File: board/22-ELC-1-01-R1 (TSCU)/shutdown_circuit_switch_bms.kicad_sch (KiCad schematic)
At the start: 7 parts, among them Q14 AO3400A

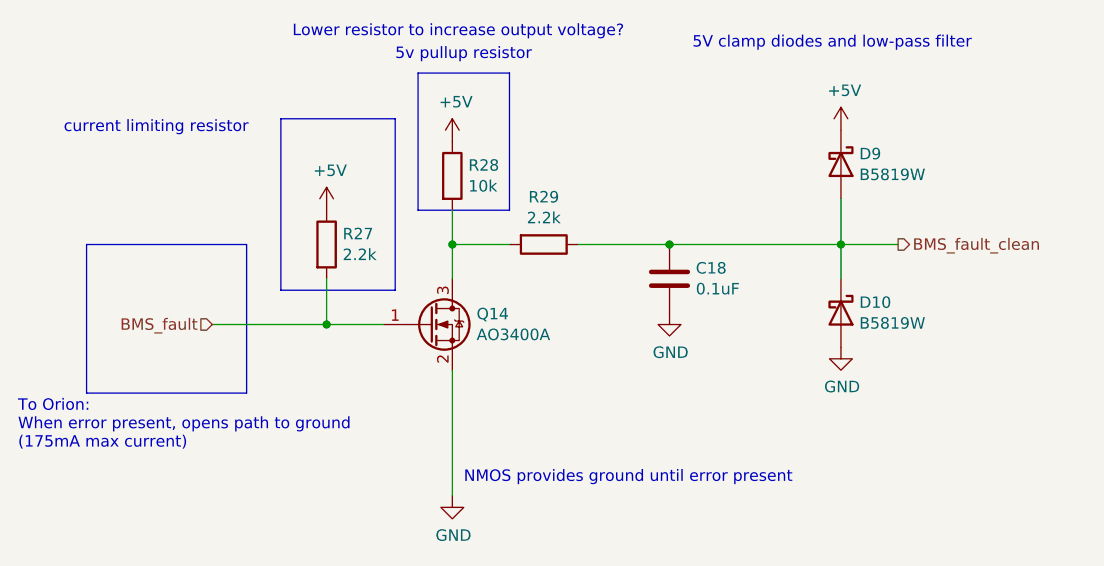
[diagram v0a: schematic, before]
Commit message: Added few LEDs
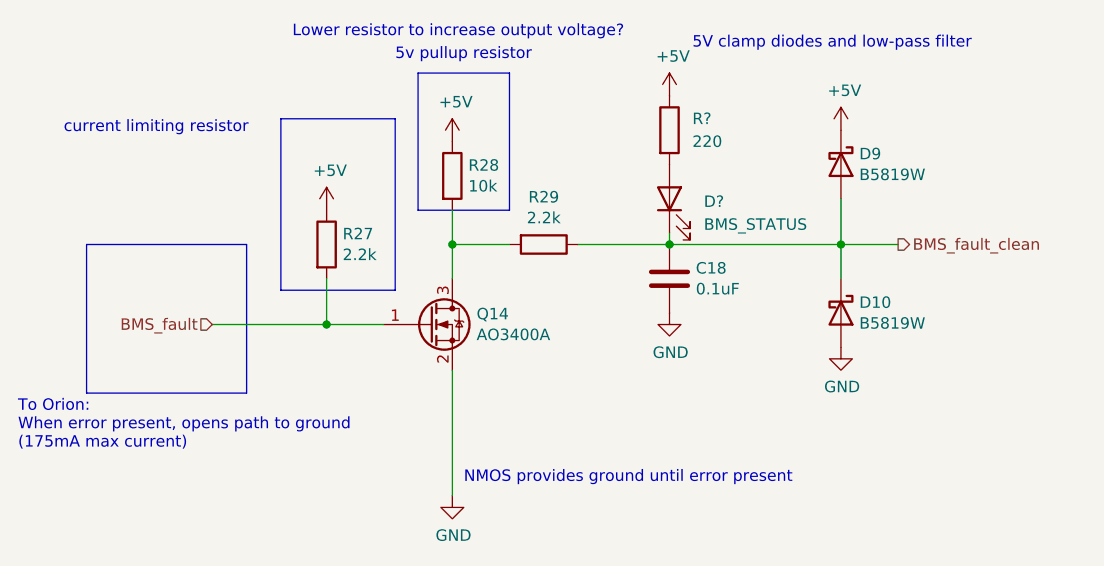
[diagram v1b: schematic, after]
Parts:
- added D?: BMS_STATUS, symbol Device:LED
- added R?: 220, symbol Device:R
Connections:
- net +5V: now also R?.1
- net BMS_fault_clean: now also D?.1 (K)
- new net: D?.2 (A), R?.2
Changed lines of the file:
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@@
+    (stroke (width 0) (type default) (color 0 0 0 0))
+  )
+  (wire (pts (xy 88.9 91.44) (xy 88.9 92.71))
     (stroke (width 0) (type default) (color 0 0 0 0))
   )
@@
     (pin "2")
   )
+  (symbol (lib_id "Device:LED") (at 88.9 87.63 90) (unit 1)
+    (in_bom yes) (on_board yes) (fields_autoplaced)
+    (property "Reference" "D?" (id 0) (at 92.71 87.9474 90)
+      (effects (font (size 1.27 1.27)) (justify right))
+    )
+    (property "Value" "BMS_STATUS" (id 1) (at 92.71 90.4874 90)
+      (effects (font (size 1.27 1.27)) (justify right))
+    )
+    (property "Footprint" "" (id 2) (at 88.9 87.63 0)
+      (effects (font (size 1.27 1.27)) hide)
+    )
+    (property "Datasheet" "~" (id 3) (at 88.9 87.63 0)
+      (effects (font (size 1.27 1.27)) hide)
+    )
+    (pin "1")
+    (pin "2")
+  )
+  (symbol (lib_id "Device:R") (at 88.9 80.01 0) (unit 1)
+    (in_bom yes) (on_board yes) (fields_autoplaced)
+    (property "Reference" "R?" (id 0) (at 91.44 78.7399 0)
+      (effects (font (size 1.27 1.27)) (justify left))
+    )
+    (property "Value" "220" (id 1) (at 91.44 81.2799 0)
+      (effects (font (size 1.27 1.27)) (justify left))
+    )
+    (property "Footprint" "" (id 2) (at 87.122 80.01 90)
+      (effects (font (size 1.27 1.27)) hide)
+    )
+    (property "Datasheet" "~" (id 3) (at 88.9 80.01 0)
+      (effects (font (size 1.27 1.27)) hide)
+    )
+    (pin "1")
+    (pin "2")
+  )
+  (symbol (lib_id "power:+5V") (at 88.9 76.2 0) (unit 1)
+    (in_bom yes) (on_board yes)
+    (property "Reference" "#PWR?" (id 0) (at 88.9 80.01 0)
+      (effects (font (size 1.27 1.27)) hide)
+    )
+    (property "Value" "+5V" (id 1) (at 89.281 71.8058 0))
+    (property "Footprint" "" (id 2) (at 88.9 76.2 0)
+      (effects (font (size 1.27 1.27)) hide)
+    )
+    (property "Datasheet" "" (id 3) (at 88.9 76.2 0)
+      (effects (font (size 1.27 1.27)) hide)
+    )
+    (pin "1")
+  )
 )

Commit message: More LEDs and test points
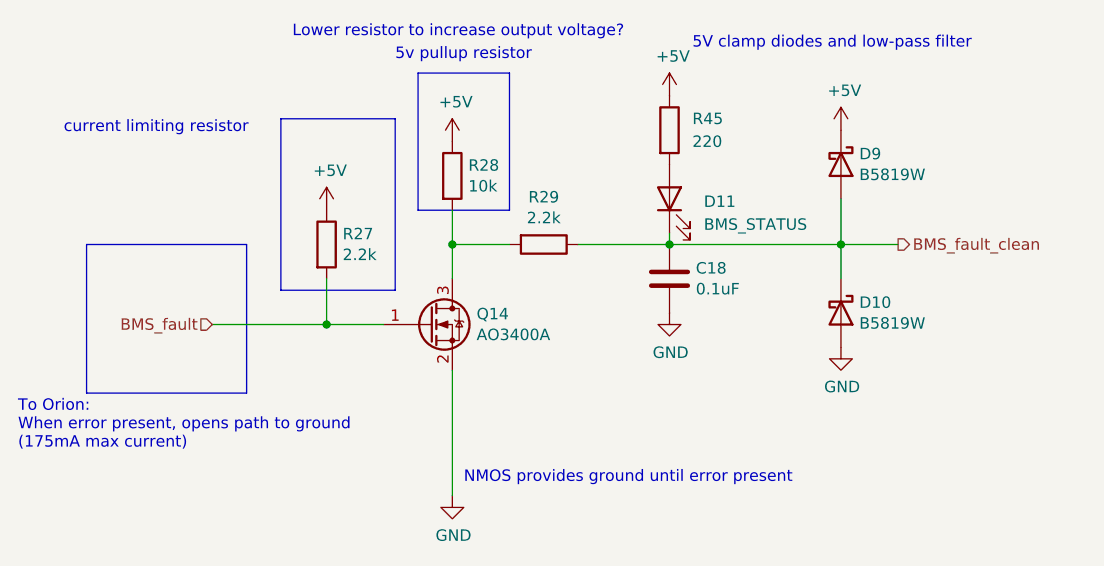
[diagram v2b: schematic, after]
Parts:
- gave numbers to parts that had none: 2
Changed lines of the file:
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@@
   (symbol (lib_id "Device:LED") (at 88.9 87.63 90) (unit 1)
     (in_bom yes) (on_board yes) (fields_autoplaced)
-    (property "Reference" "D?" (id 0) (at 92.71 87.9474 90)
+    (property "Reference" "D11" (id 0) (at 92.71 87.9474 90)
       (effects (font (size 1.27 1.27)) (justify right))
     )
@@
   (symbol (lib_id "Device:R") (at 88.9 80.01 0) (unit 1)
     (in_bom yes) (on_board yes) (fields_autoplaced)
-    (property "Reference" "R?" (id 0) (at 91.44 78.7399 0)
+    (property "Reference" "R45" (id 0) (at 91.44 78.7399 0)
       (effects (font (size 1.27 1.27)) (justify left))
     )
@@
   (symbol (lib_id "power:+5V") (at 88.9 76.2 0) (unit 1)
     (in_bom yes) (on_board yes)
-    (property "Reference" "#PWR?" (id 0) (at 88.9 80.01 0)
+    (property "Reference" "#PWR0104" (id 0) (at 88.9 80.01 0)
       (effects (font (size 1.27 1.27)) hide)
     )

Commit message: Ready for review
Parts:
- renumbered C18 to C1, D11 to D2, D9 to D3, D10 to D4, Q14 to Q1, R27 to R1, R28 to R2, R29 to R3, R45 to R4
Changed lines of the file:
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@@
   (symbol (lib_id "power:+5V") (at 50.8 88.9 0) (unit 1)
     (in_bom yes) (on_board yes)
-    (property "Reference" "#PWR02" (id 0) (at 50.8 92.71 0)
+    (property "Reference" "#PWR010" (id 0) (at 50.8 92.71 0)
       (effects (font (size 1.27 1.27)) hide)
     )
@@
   (symbol (lib_id "Device:R") (at 50.8 92.71 0) (unit 1)
     (in_bom yes) (on_board yes)
-    (property "Reference" "R27" (id 0) (at 52.578 91.5416 0)
+    (property "Reference" "R1" (id 0) (at 52.578 91.5416 0)
       (effects (font (size 1.27 1.27)) (justify left))
     )
@@
   (symbol (lib_id "Device:R") (at 74.93 92.71 270) (unit 1)
     (in_bom yes) (on_board yes)
-    (property "Reference" "R29" (id 0) (at 74.93 87.4522 90))
+    (property "Reference" "R3" (id 0) (at 74.93 87.4522 90))
     (property "Value" "2.2k" (id 1) (at 74.93 89.7636 90))
     (property "Footprint" "Resistor_SMD:R_0603_1608Metric_Pad0.98x0.95mm_HandSolder" (id 2) (at 74.93 90.932 90)
@@
   (symbol (lib_id "Device:C") (at 88.9 96.52 0) (unit 1)
     (in_bom yes) (on_board yes)
-    (property "Reference" "C18" (id 0) (at 91.821 95.3516 0)
+    (property "Reference" "C1" (id 0) (at 91.821 95.3516 0)
       (effects (font (size 1.27 1.27)) (justify left))
     )
@@
   (symbol (lib_id "power:GND") (at 88.9 100.33 0) (unit 1)
     (in_bom yes) (on_board yes)
-    (property "Reference" "#PWR076" (id 0) (at 88.9 106.68 0)
+    (property "Reference" "#PWR014" (id 0) (at 88.9 106.68 0)
       (effects (font (size 1.27 1.27)) hide)
     )
@@
   (symbol (lib_id "power:GND") (at 107.95 104.14 0) (unit 1)
     (in_bom yes) (on_board yes)
-    (property "Reference" "#PWR079" (id 0) (at 107.95 110.49 0)
+    (property "Reference" "#PWR016" (id 0) (at 107.95 110.49 0)
       (effects (font (size 1.27 1.27)) hide)
     )
@@
   (symbol (lib_id "power:+5V") (at 107.95 80.01 0) (unit 1)
     (in_bom yes) (on_board yes)
-    (property "Reference" "#PWR078" (id 0) (at 107.95 83.82 0)
+    (property "Reference" "#PWR015" (id 0) (at 107.95 83.82 0)
       (effects (font (size 1.27 1.27)) hide)
     )
@@
   (symbol (lib_id "power:GND") (at 64.77 120.65 0) (unit 1)
     (in_bom yes) (on_board yes)
-    (property "Reference" "#PWR074" (id 0) (at 64.77 127 0)
+    (property "Reference" "#PWR012" (id 0) (at 64.77 127 0)
       (effects (font (size 1.27 1.27)) hide)
     )
@@
   (symbol (lib_id "Device:R") (at 64.77 85.09 0) (unit 1)
     (in_bom yes) (on_board yes)
-    (property "Reference" "R28" (id 0) (at 66.548 83.9216 0)
+    (property "Reference" "R2" (id 0) (at 66.548 83.9216 0)
       (effects (font (size 1.27 1.27)) (justify left))
     )
@@
   (symbol (lib_id "power:+5V") (at 64.77 81.28 0) (unit 1)
     (in_bom yes) (on_board yes)
-    (property "Reference" "#PWR05" (id 0) (at 64.77 85.09 0)
+    (property "Reference" "#PWR011" (id 0) (at 64.77 85.09 0)
       (effects (font (size 1.27 1.27)) hide)
     )
@@
   (symbol (lib_id "Device:Q_NMOS_GSD") (at 62.23 101.6 0) (unit 1)
     (in_bom yes) (on_board yes)
-    (property "Reference" "Q14" (id 0) (at 67.4624 100.4316 0)
+    (property "Reference" "Q1" (id 0) (at 67.4624 100.4316 0)
       (effects (font (size 1.27 1.27)) (justify left))
     )
@@
   (symbol (lib_id "Device:D_Schottky") (at 107.95 83.82 270) (unit 1)
     (in_bom yes) (on_board yes)
-    (property "Reference" "D9" (id 0) (at 109.982 82.6516 90)
+    (property "Reference" "D3" (id 0) (at 109.982 82.6516 90)
       (effects (font (size 1.27 1.27)) (justify left))
     )
@@
   (symbol (lib_id "Device:D_Schottky") (at 107.95 100.33 270) (unit 1)
     (in_bom yes) (on_board yes)
-    (property "Reference" "D10" (id 0) (at 109.982 99.1616 90)
+    (property "Reference" "D4" (id 0) (at 109.982 99.1616 90)
       (effects (font (size 1.27 1.27)) (justify left))
     )
@@
   (symbol (lib_id "Device:LED") (at 88.9 87.63 90) (unit 1)
     (in_bom yes) (on_board yes) (fields_autoplaced)
-    (property "Reference" "D11" (id 0) (at 92.71 87.9474 90)
+    (property "Reference" "D2" (id 0) (at 92.71 87.9474 90)
       (effects (font (size 1.27 1.27)) (justify right))
     )
@@
   (symbol (lib_id "Device:R") (at 88.9 80.01 0) (unit 1)
     (in_bom yes) (on_board yes) (fields_autoplaced)
-    (property "Reference" "R45" (id 0) (at 91.44 78.7399 0)
+    (property "Reference" "R4" (id 0) (at 91.44 78.7399 0)
       (effects (font (size 1.27 1.27)) (justify left))
     )
@@
   (symbol (lib_id "power:+5V") (at 88.9 76.2 0) (unit 1)
     (in_bom yes) (on_board yes)
-    (property "Reference" "#PWR0104" (id 0) (at 88.9 80.01 0)
-      (effects (font (size 1.27 1.27)) hide)
-    )
+    (property "Reference" "#PWR013" (id 0) (at 88.9 80.01 0)
+      (effects (font (size 1.27 1.27)) hide)
+    )

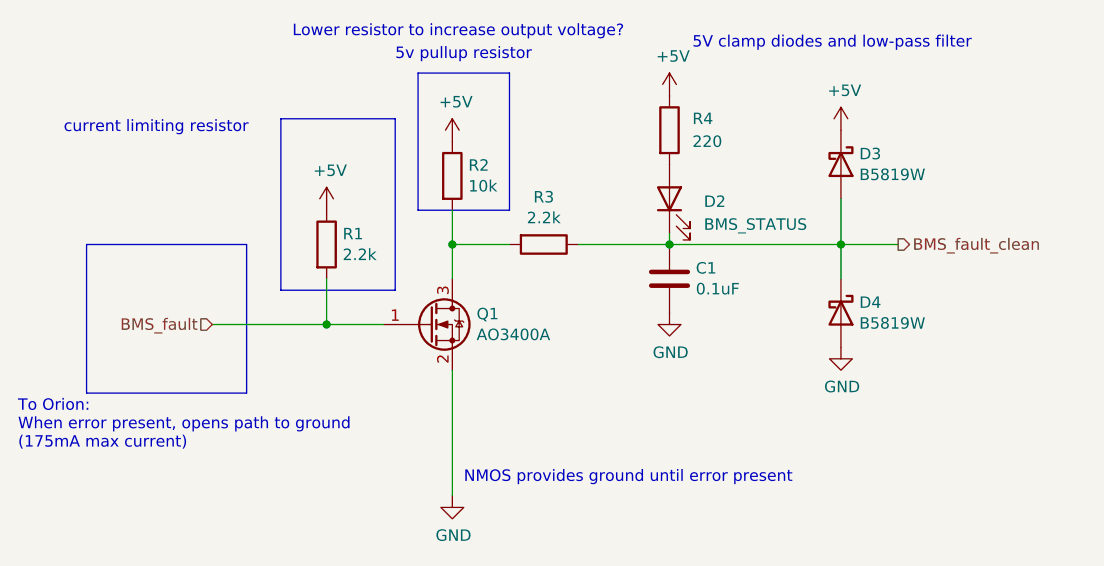
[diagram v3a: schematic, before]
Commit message: All good except need to switch everything to accepting 24v power
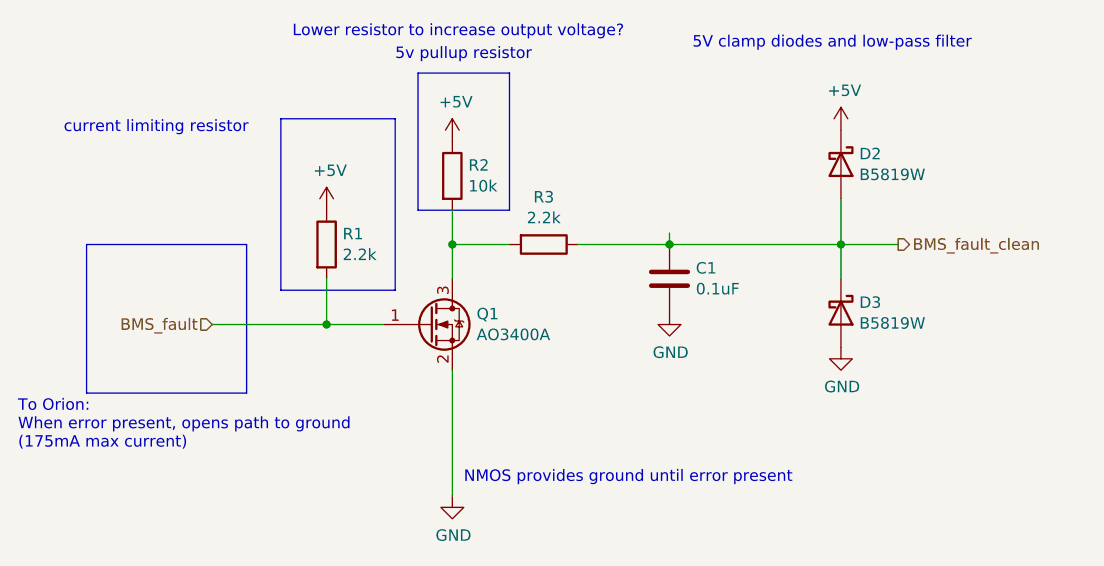
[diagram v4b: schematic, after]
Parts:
- removed D2: BMS_STATUS, symbol Device:LED
- removed R4: 220, symbol Device:R
- renumbered D3 to D2, D4 to D3
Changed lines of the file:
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@@
   (symbol (lib_id "power:+5V") (at 50.8 88.9 0) (unit 1)
     (in_bom yes) (on_board yes)
-    (property "Reference" "#PWR010" (id 0) (at 50.8 92.71 0)
+    (property "Reference" "#PWR012" (id 0) (at 50.8 92.71 0)
       (effects (font (size 1.27 1.27)) hide)
     )
@@
   (symbol (lib_id "power:GND") (at 88.9 100.33 0) (unit 1)
     (in_bom yes) (on_board yes)
-    (property "Reference" "#PWR014" (id 0) (at 88.9 106.68 0)
+    (property "Reference" "#PWR015" (id 0) (at 88.9 106.68 0)
       (effects (font (size 1.27 1.27)) hide)
     )
@@
   (symbol (lib_id "power:GND") (at 107.95 104.14 0) (unit 1)
     (in_bom yes) (on_board yes)
-    (property "Reference" "#PWR016" (id 0) (at 107.95 110.49 0)
+    (property "Reference" "#PWR017" (id 0) (at 107.95 110.49 0)
       (effects (font (size 1.27 1.27)) hide)
     )
@@
   (symbol (lib_id "power:+5V") (at 107.95 80.01 0) (unit 1)
     (in_bom yes) (on_board yes)
-    (property "Reference" "#PWR015" (id 0) (at 107.95 83.82 0)
+    (property "Reference" "#PWR016" (id 0) (at 107.95 83.82 0)
       (effects (font (size 1.27 1.27)) hide)
     )
@@
   (symbol (lib_id "power:GND") (at 64.77 120.65 0) (unit 1)
     (in_bom yes) (on_board yes)
-    (property "Reference" "#PWR012" (id 0) (at 64.77 127 0)
+    (property "Reference" "#PWR014" (id 0) (at 64.77 127 0)
       (effects (font (size 1.27 1.27)) hide)
     )
@@
   (symbol (lib_id "power:+5V") (at 64.77 81.28 0) (unit 1)
     (in_bom yes) (on_board yes)
-    (property "Reference" "#PWR011" (id 0) (at 64.77 85.09 0)
+    (property "Reference" "#PWR013" (id 0) (at 64.77 85.09 0)
       (effects (font (size 1.27 1.27)) hide)
     )
@@
   (symbol (lib_id "Device:D_Schottky") (at 107.95 83.82 270) (unit 1)
     (in_bom yes) (on_board yes)
-    (property "Reference" "D3" (id 0) (at 109.982 82.6516 90)
+    (property "Reference" "D2" (id 0) (at 109.982 82.6516 90)
       (effects (font (size 1.27 1.27)) (justify left))
     )
@@
   (symbol (lib_id "Device:D_Schottky") (at 107.95 100.33 270) (unit 1)
     (in_bom yes) (on_board yes)
-    (property "Reference" "D4" (id 0) (at 109.982 99.1616 90)
+    (property "Reference" "D3" (id 0) (at 109.982 99.1616 90)
       (effects (font (size 1.27 1.27)) (justify left))
     )
@@
     (pin "2")
   )
-  (symbol (lib_id "Device:LED") (at 88.9 87.63 90) (unit 1)
-    (in_bom yes) (on_board yes) (fields_autoplaced)
-    (property "Reference" "D2" (id 0) (at 92.71 87.9474 90)
-      (effects (font (size 1.27 1.27)) (justify right))
-    )
-    (property "Value" "BMS_STATUS" (id 1) (at 92.71 90.4874 90)
-      (effects (font (size 1.27 1.27)) (justify right))
-    )
-    (property "Footprint" "" (id 2) (at 88.9 87.63 0)
-      (effects (font (size 1.27 1.27)) hide)
-    )
-    (property "Datasheet" "~" (id 3) (at 88.9 87.63 0)
-      (effects (font (size 1.27 1.27)) hide)
-    )
-    (pin "1")
-    (pin "2")
-  )
-  (symbol (lib_id "Device:R") (at 88.9 80.01 0) (unit 1)
-    (in_bom yes) (on_board yes) (fields_autoplaced)
-    (property "Reference" "R4" (id 0) (at 91.44 78.7399 0)
-      (effects (font (size 1.27 1.27)) (justify left))
-    )
-    (property "Value" "220" (id 1) (at 91.44 81.2799 0)
-      (effects (font (size 1.27 1.27)) (justify left))
-    )
-    (property "Footprint" "" (id 2) (at 87.122 80.01 90)
-      (effects (font (size 1.27 1.27)) hide)
-    )
-    (property "Datasheet" "~" (id 3) (at 88.9 80.01 0)
-      (effects (font (size 1.27 1.27)) hide)
-    )
-    (pin "1")
-    (pin "2")
-  )
-  (symbol (lib_id "power:+5V") (at 88.9 76.2 0) (unit 1)
-    (in_bom yes) (on_board yes)
-    (property "Reference" "#PWR013" (id 0) (at 88.9 80.01 0)
-      (effects (font (size 1.27 1.27)) hide)
-    )
-    (property "Value" "+5V" (id 1) (at 89.281 71.8058 0))
-    (property "Footprint" "" (id 2) (at 88.9 76.2 0)
-      (effects (font (size 1.27 1.27)) hide)
-    )
-    (property "Datasheet" "" (id 3) (at 88.9 76.2 0)
-      (effects (font (size 1.27 1.27)) hide)
-    )
-    (pin "1")
-  )
 )

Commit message: Finalized schematic, started board layout
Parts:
- C1: footprint Capacitor_SMD:C_0603_1608Metric_Pad1.08x0.95mm_HandSolder -> Capacitor_SMD:C_0402_1005Metric
- R1, R2, R3: footprint Resistor_SMD:R_0603_1608Metric_Pad0.98x0.95mm_HandSolder -> FixedTextSizes:R_0402_1005Metric
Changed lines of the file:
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@@
   (symbol (lib_id "power:+5V") (at 50.8 88.9 0) (unit 1)
     (in_bom yes) (on_board yes)
-    (property "Reference" "#PWR012" (id 0) (at 50.8 92.71 0)
+    (property "Reference" "#PWR011" (id 0) (at 50.8 92.71 0)
       (effects (font (size 1.27 1.27)) hide)
     )
@@
       (effects (font (size 1.27 1.27)) (justify left))
     )
-    (property "Footprint" "Resistor_SMD:R_0603_1608Metric_Pad0.98x0.95mm_HandSolder" (id 2) (at 49.022 92.71 90)
+    (property "Footprint" "FixedTextSizes:R_0402_1005Metric" (id 2) (at 49.022 92.71 90)
       (effects (font (size 1.27 1.27)) hide)
     )
@@
     (property "Reference" "R3" (id 0) (at 74.93 87.4522 90))
     (property "Value" "2.2k" (id 1) (at 74.93 89.7636 90))
-    (property "Footprint" "Resistor_SMD:R_0603_1608Metric_Pad0.98x0.95mm_HandSolder" (id 2) (at 74.93 90.932 90)
+    (property "Footprint" "FixedTextSizes:R_0402_1005Metric" (id 2) (at 74.93 90.932 90)
       (effects (font (size 1.27 1.27)) hide)
     )
@@
       (effects (font (size 1.27 1.27)) (justify left))
     )
-    (property "Footprint" "Capacitor_SMD:C_0603_1608Metric_Pad1.08x0.95mm_HandSolder" (id 2) (at 89.8652 100.33 0)
+    (property "Footprint" "Capacitor_SMD:C_0402_1005Metric" (id 2) (at 89.8652 100.33 0)
       (effects (font (size 1.27 1.27)) hide)
     )
@@
   (symbol (lib_id "power:GND") (at 88.9 100.33 0) (unit 1)
     (in_bom yes) (on_board yes)
-    (property "Reference" "#PWR015" (id 0) (at 88.9 106.68 0)
+    (property "Reference" "#PWR014" (id 0) (at 88.9 106.68 0)
       (effects (font (size 1.27 1.27)) hide)
     )
@@
   (symbol (lib_id "power:GND") (at 107.95 104.14 0) (unit 1)
     (in_bom yes) (on_board yes)
-    (property "Reference" "#PWR017" (id 0) (at 107.95 110.49 0)
+    (property "Reference" "#PWR016" (id 0) (at 107.95 110.49 0)
       (effects (font (size 1.27 1.27)) hide)
     )
@@
   (symbol (lib_id "power:+5V") (at 107.95 80.01 0) (unit 1)
     (in_bom yes) (on_board yes)
-    (property "Reference" "#PWR016" (id 0) (at 107.95 83.82 0)
+    (property "Reference" "#PWR015" (id 0) (at 107.95 83.82 0)
       (effects (font (size 1.27 1.27)) hide)
     )
@@
   (symbol (lib_id "power:GND") (at 64.77 120.65 0) (unit 1)
     (in_bom yes) (on_board yes)
-    (property "Reference" "#PWR014" (id 0) (at 64.77 127 0)
+    (property "Reference" "#PWR013" (id 0) (at 64.77 127 0)
       (effects (font (size 1.27 1.27)) hide)
     )
@@
       (effects (font (size 1.27 1.27)) (justify left))
     )
-    (property "Footprint" "Resistor_SMD:R_0603_1608Metric_Pad0.98x0.95mm_HandSolder" (id 2) (at 62.992 85.09 90)
+    (property "Footprint" "FixedTextSizes:R_0402_1005Metric" (id 2) (at 62.992 85.09 90)
       (effects (font (size 1.27 1.27)) hide)
     )
@@
   (symbol (lib_id "power:+5V") (at 64.77 81.28 0) (unit 1)
     (in_bom yes) (on_board yes)
-    (property "Reference" "#PWR013" (id 0) (at 64.77 85.09 0)
+    (property "Reference" "#PWR012" (id 0) (at 64.77 85.09 0)
       (effects (font (size 1.27 1.27)) hide)
     )
